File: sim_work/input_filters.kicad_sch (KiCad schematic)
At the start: 64 parts

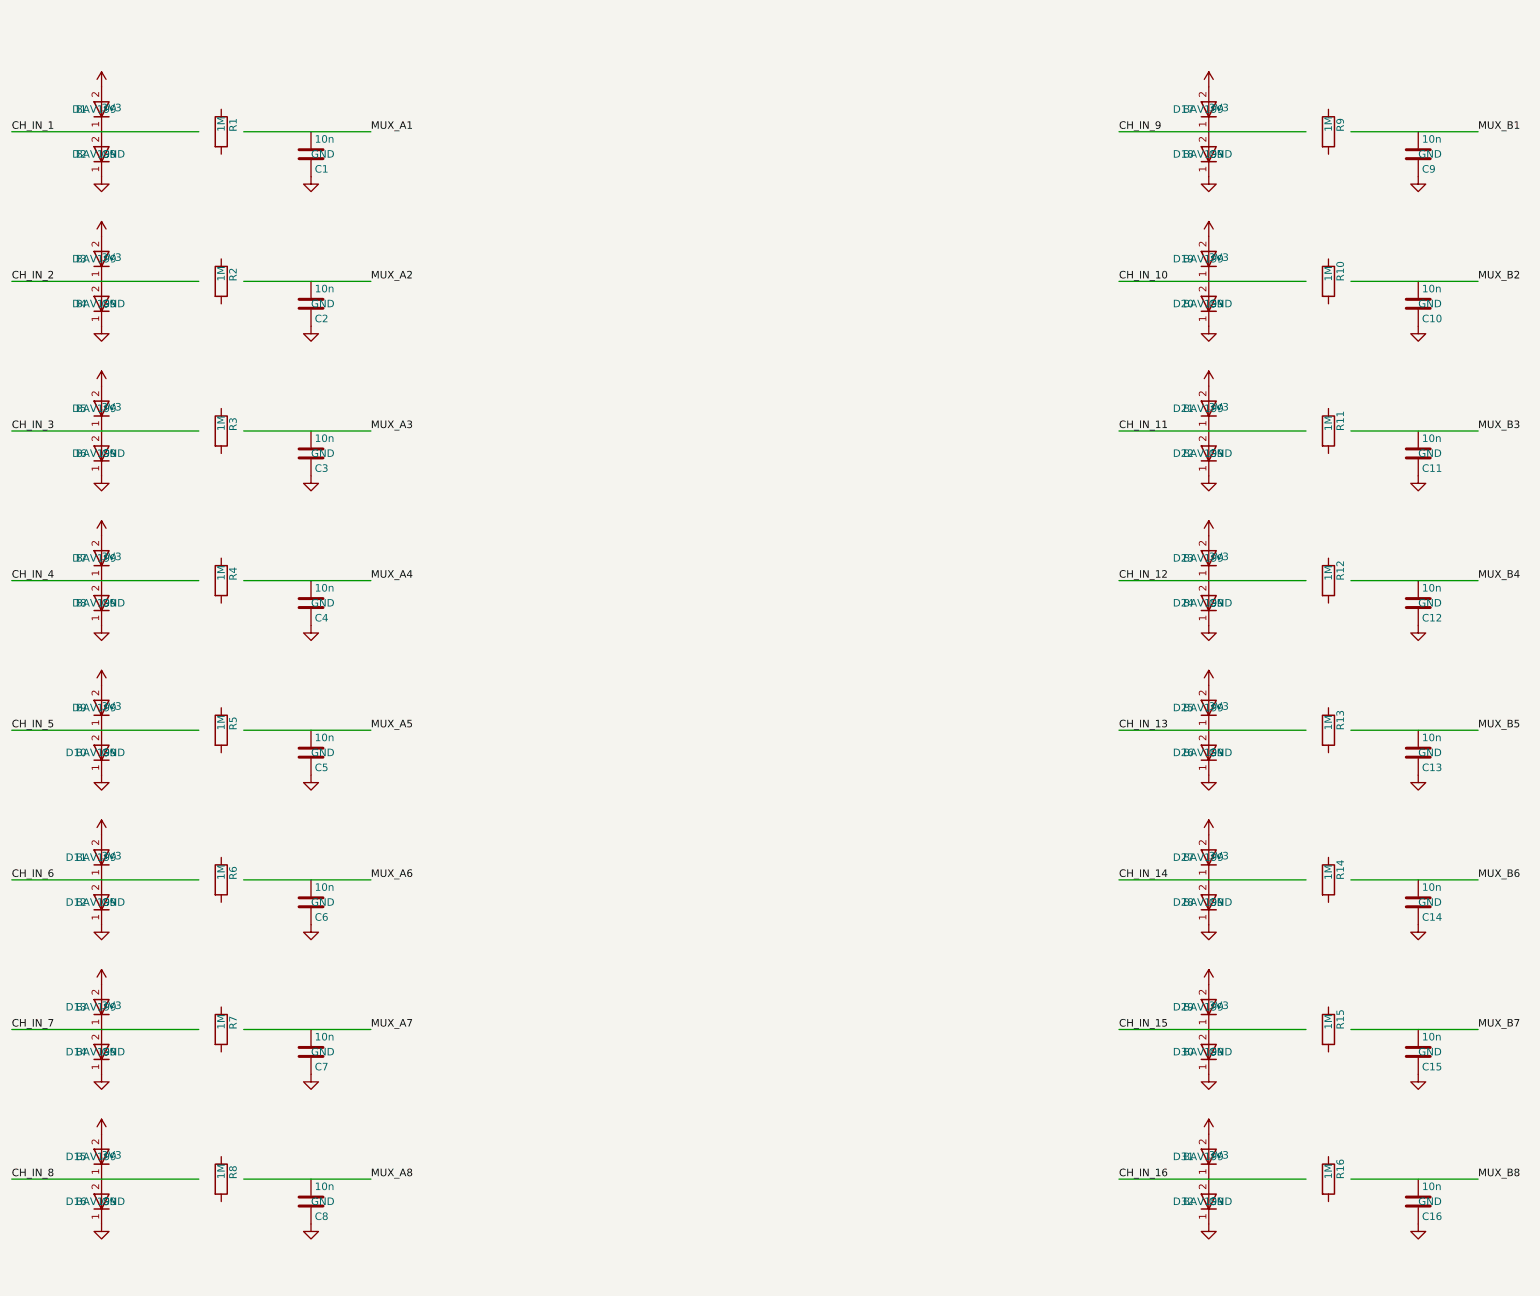
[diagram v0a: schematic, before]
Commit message: Per-block PDF schematics: 6 oscillator + 6 TIA blocks with merged PDFs
Add individual A4 schematic generation for each functional circuit block:
- Oscillator: summing amp, integrator 1/2, RMS detector, power supply, MCU
- TIA: input filters, analog mux, mux TIA, relay ladder, MCU section, electrometer
- merge_pdfs() helper using PyMuPDF for multi-page output
- CLI commands: osc_blocks, tia_blocks
- All blocks verified: 0 wire crossings, complete pin connectivity

Co-Authored-By: Claude Opus 4.6 <noreply@anthropic.com>
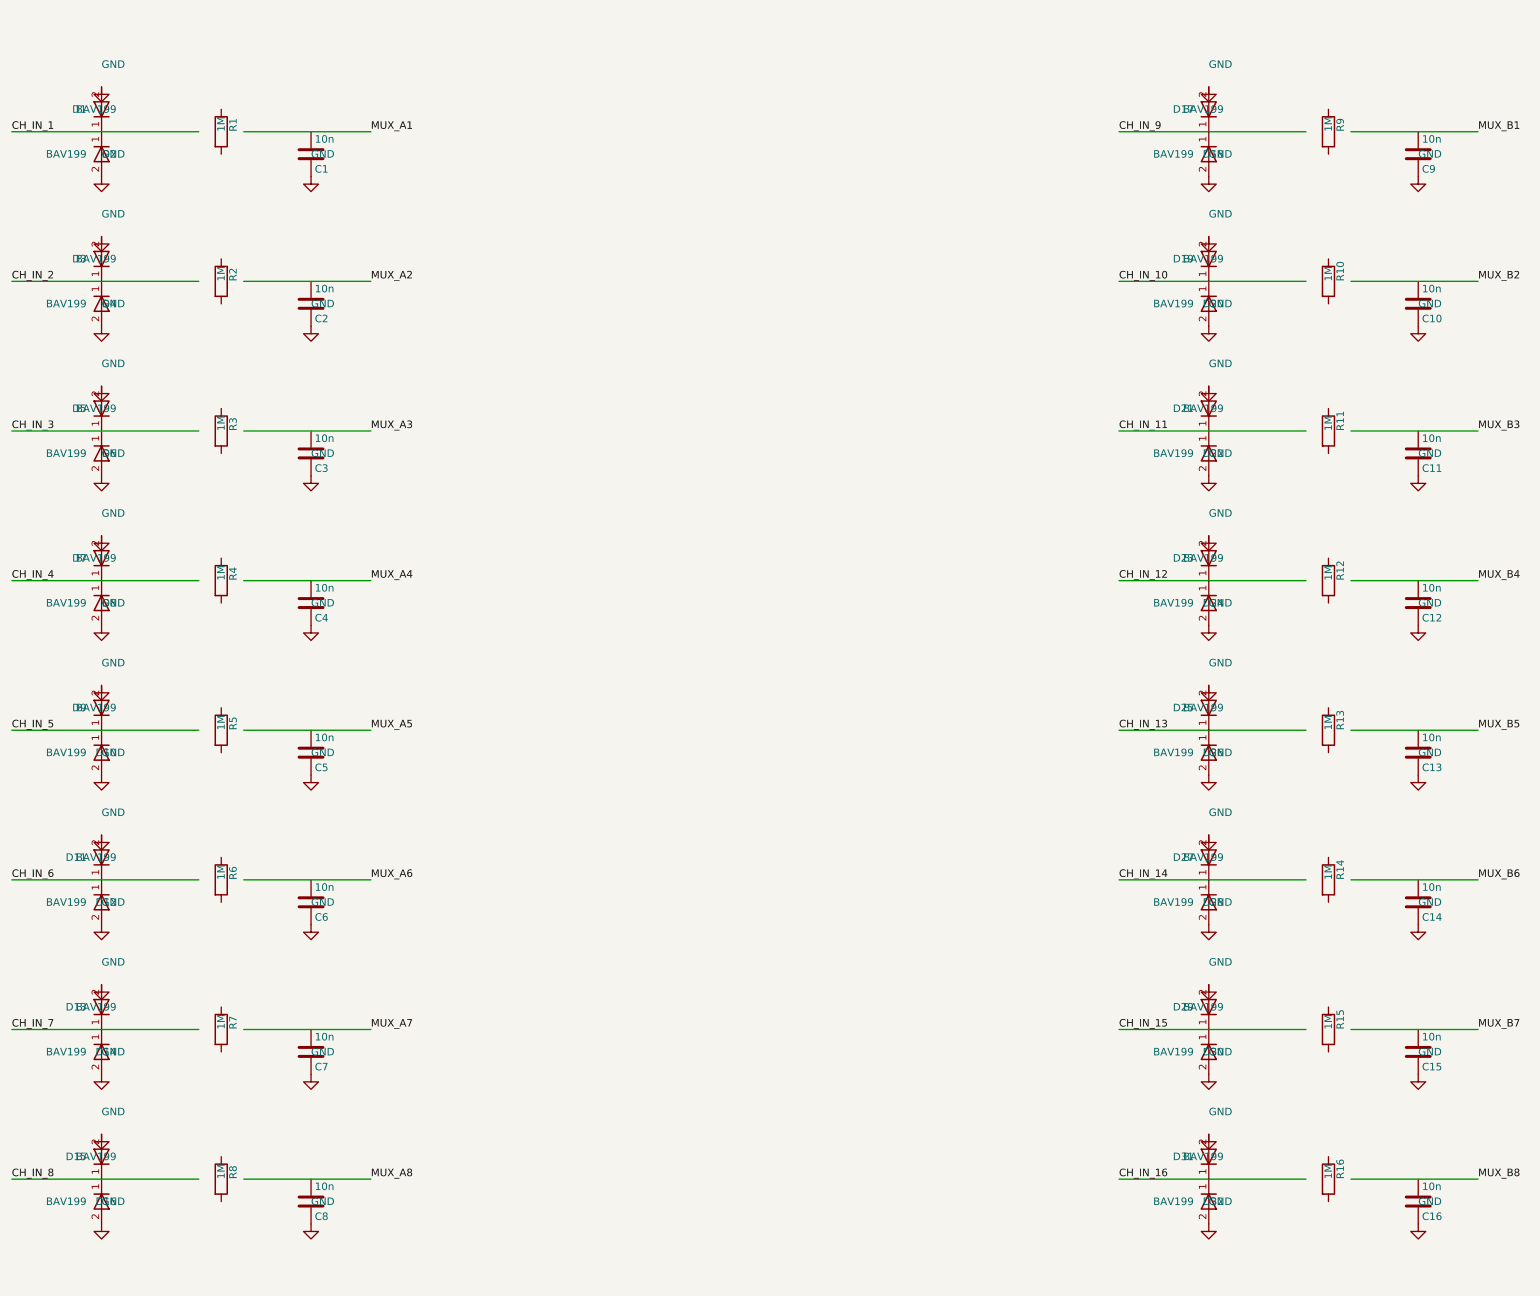
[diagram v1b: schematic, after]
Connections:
- net 3V3 is gone; now on net GND: D1.2 (A), D11.2 (A), D13.2 (A), D15.2 (A), D17.2 (A), D19.2 (A), D21.2 (A), D23.2 (A), D25.2 (A), D27.2 (A), D29.2 (A), D3.2 (A), D31.2 (A), D5.2 (A), D7.2 (A), D9.2 (A)
- net GND: now also D10.2 (A), D12.2 (A), D14.2 (A), D16.2 (A), D18.2 (A), D2.2 (A), D20.2 (A), D22.2 (A), D24.2 (A), D26.2 (A), D28.2 (A), D30.2 (A), D32.2 (A), D4.2 (A), D6.2 (A), D8.2 (A); no longer D10.1 (K), D12.1 (K), D14.1 (K), D16.1 (K), D18.1 (K), D2.1 (K), D20.1 (K), D22.1 (K), D24.1 (K), D26.1 (K), D28.1 (K), D30.1 (K), D32.1 (K), D4.1 (K), D6.1 (K), D8.1 (K)
- net at D15.1 (K): now also D16.1 (K); no longer D16.2 (A)
- net at D11.1 (K): now also D12.1 (K); no longer D12.2 (A)
- net at D21.1 (K): now also D22.1 (K); no longer D22.2 (A)
- net at D13.1 (K): now also D14.1 (K); no longer D14.2 (A)
- net at D1.1 (K): now also D2.1 (K); no longer D2.2 (A)
- net at D7.1 (K): now also D8.1 (K); no longer D8.2 (A)
- net at D19.1 (K): now also D20.1 (K); no longer D20.2 (A)
- net at D27.1 (K): now also D28.1 (K); no longer D28.2 (A)
- net at D23.1 (K): now also D24.1 (K); no longer D24.2 (A)
- net at D29.1 (K): now also D30.1 (K); no longer D30.2 (A)
- net at D9.1 (K): now also D10.1 (K); no longer D10.2 (A)
- net at D25.1 (K): now also D26.1 (K); no longer D26.2 (A)
- net at D31.1 (K): now also D32.1 (K); no longer D32.2 (A)
- net at D17.1 (K): now also D18.1 (K); no longer D18.2 (A)
- net at D3.1 (K): now also D4.1 (K); no longer D4.2 (A)
- net at D5.1 (K): now also D6.1 (K); no longer D6.2 (A)

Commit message: Fix schematic connections, add docs and repo portability
- Input filters: R rotation=90 (horizontal), ESD diode rotations fixed,
  junction dots at cathode-signal connection, wires to GND symbols
- Relay ladder: flyback diode rotation 270->90 (K top, A bottom)
- Electrometer/Mux TIA: 4 junction dots each at T-junctions
- AD636 RMS detector: proper IC box with pin labels replaces text-only
- Oscillator blocks: D_Zener symbol, L-shaped cathode routing
- TIA blocks: title/function annotations on all 5 blocks
- New: requirements.txt, docs/oscillator_guide.md
- D_Zener.kicad_sym added to bundled symbols/
- .gitignore updated for docs/ and requirements.txt
- README updated with pip install -r requirements.txt
- PROJECT.md session 9 changelog
- SimGUI builds clean (0 errors)

Co-Authored-By: Claude Opus 4.6 <noreply@anthropic.com>
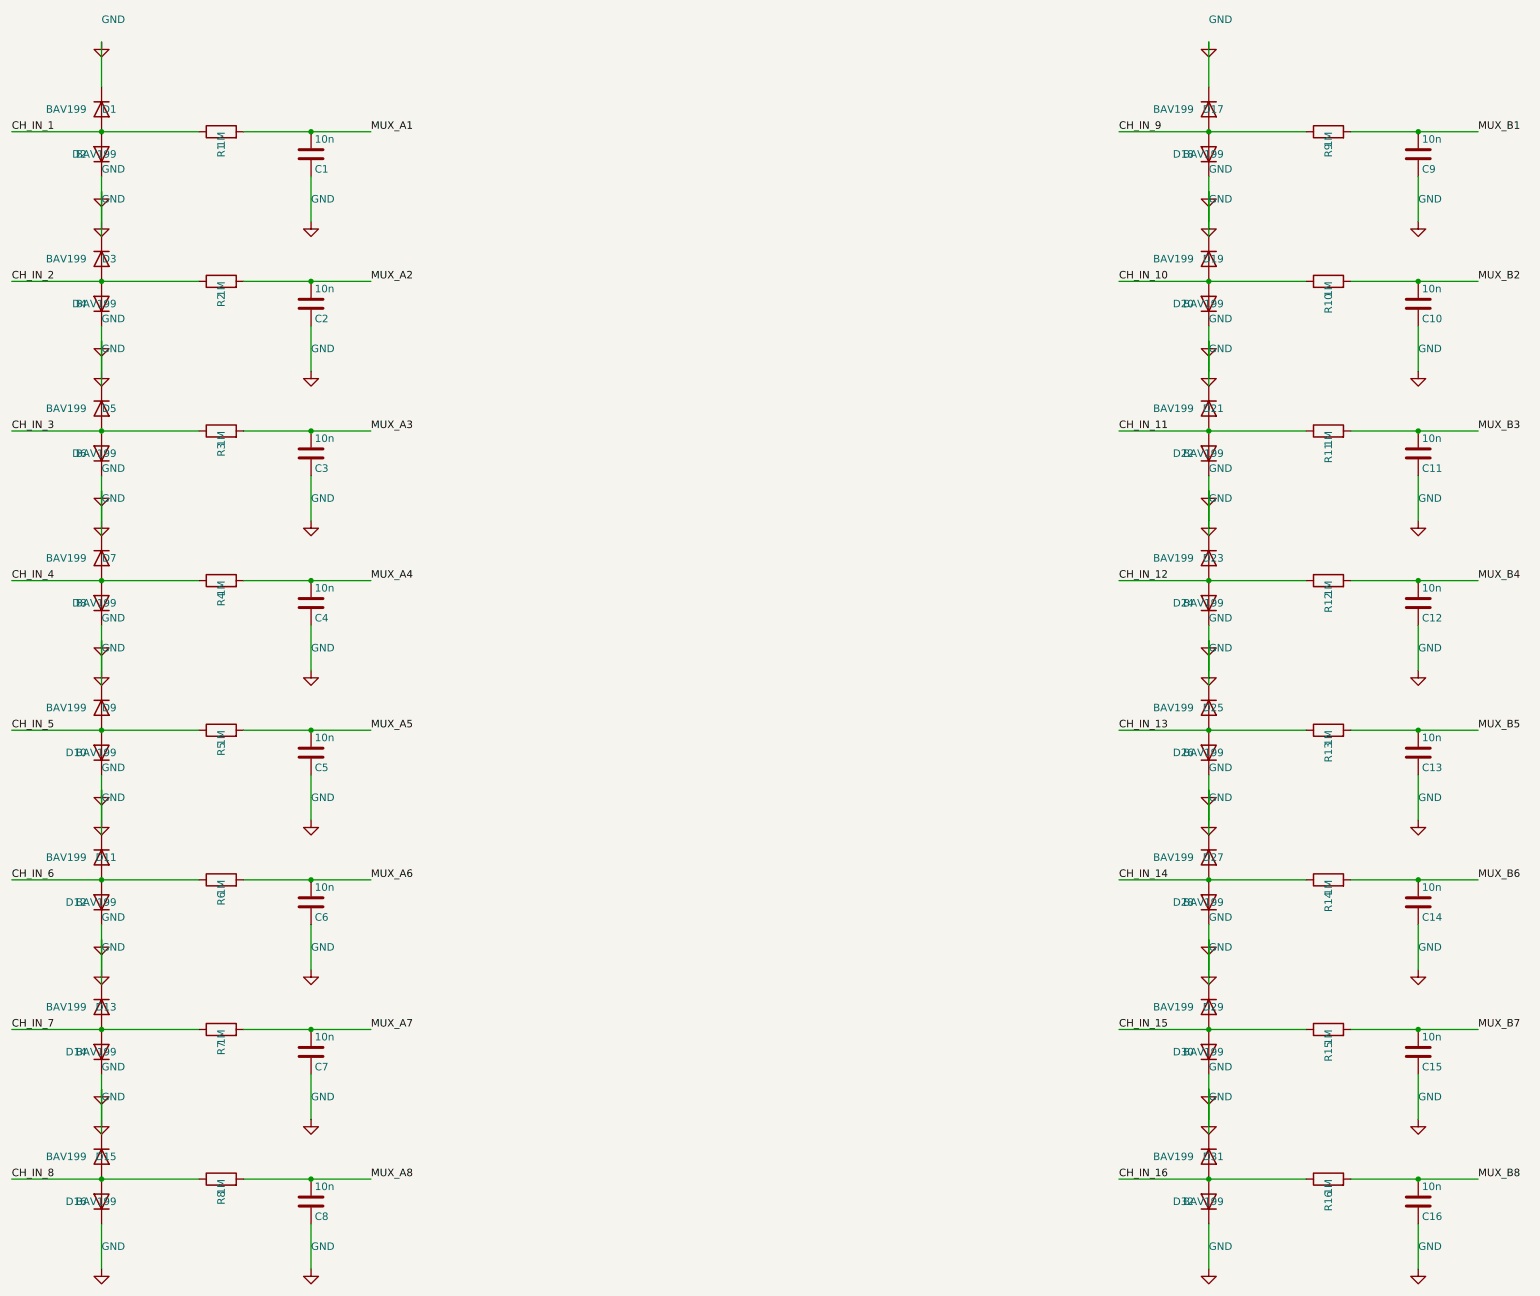
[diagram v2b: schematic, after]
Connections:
- net CH_IN_1: now also D1.2 (A), D2.2 (A), R1.1
- net CH_IN_10: now also D19.2 (A), D20.2 (A), R10.1
- net CH_IN_11: now also D21.2 (A), D22.2 (A), R11.1
- net CH_IN_12: now also D23.2 (A), D24.2 (A), R12.1
- net CH_IN_13: now also D25.2 (A), D26.2 (A), R13.1
- net CH_IN_14: now also D27.2 (A), D28.2 (A), R14.1
- net CH_IN_15: now also D29.2 (A), D30.2 (A), R15.1
- net CH_IN_16: now also D31.2 (A), D32.2 (A), R16.1
- net CH_IN_2: now also D3.2 (A), D4.2 (A), R2.1
- net CH_IN_3: now also D5.2 (A), D6.2 (A), R3.1
- net CH_IN_4: now also D7.2 (A), D8.2 (A), R4.1
- net CH_IN_5: now also D10.2 (A), D9.2 (A), R5.1
- net CH_IN_6: now also D11.2 (A), D12.2 (A), R6.1
- net CH_IN_7: now also D13.2 (A), D14.2 (A), R7.1
- net CH_IN_8: now also D15.2 (A), D16.2 (A), R8.1
- net CH_IN_9: now also D17.2 (A), D18.2 (A), R9.1
- net GND: now also D1.1 (K), D10.1 (K), D11.1 (K), D12.1 (K), D13.1 (K), D14.1 (K), D15.1 (K), D16.1 (K), D17.1 (K), D18.1 (K), D19.1 (K), D2.1 (K), D20.1 (K), D21.1 (K), D22.1 (K), D23.1 (K), D24.1 (K), D25.1 (K), D26.1 (K), D27.1 (K), D28.1 (K), D29.1 (K), D3.1 (K), D30.1 (K), D31.1 (K), D32.1 (K), D4.1 (K), D5.1 (K), D6.1 (K), D7.1 (K), D8.1 (K), D9.1 (K); no longer D1.2 (A), D10.2 (A), D11.2 (A), D12.2 (A), D13.2 (A), D14.2 (A), D15.2 (A), D16.2 (A), D17.2 (A), D18.2 (A), D19.2 (A), D2.2 (A), D20.2 (A), D21.2 (A), D22.2 (A), D23.2 (A), D24.2 (A), D25.2 (A), D26.2 (A), D27.2 (A), D28.2 (A), D29.2 (A), D3.2 (A), D30.2 (A), D31.2 (A), D32.2 (A), D4.2 (A), D5.2 (A), D6.2 (A), D7.2 (A), D8.2 (A), D9.2 (A)
- net MUX_A1: now also C1.1, R1.2
- net MUX_A2: now also C2.1, R2.2
- net MUX_A3: now also C3.1, R3.2
- net MUX_A4: now also C4.1, R4.2
- net MUX_A5: now also C5.1, R5.2
- net MUX_A6: now also C6.1, R6.2
- net MUX_A7: now also C7.1, R7.2
- net MUX_A8: now also C8.1, R8.2
- net MUX_B1: now also C9.1, R9.2
- net MUX_B2: now also C10.1, R10.2
- net MUX_B3: now also C11.1, R11.2
- net MUX_B4: now also C12.1, R12.2
- net MUX_B5: now also C13.1, R13.2
- net MUX_B6: now also C14.1, R14.2
- net MUX_B7: now also C15.1, R15.2
- net MUX_B8: now also C16.1, R16.2

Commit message: Tighten input filter layout: resistor closer to ESD diodes
Moved R from col_x+14G to col_x+9G (3.81mm gap vs 16.5mm) so the
diode-to-resistor connection is visually clear in rendered PDFs.
Capacitor and MUX label shifted left proportionally.

Co-Authored-By: Claude Opus 4.6 <noreply@anthropic.com>
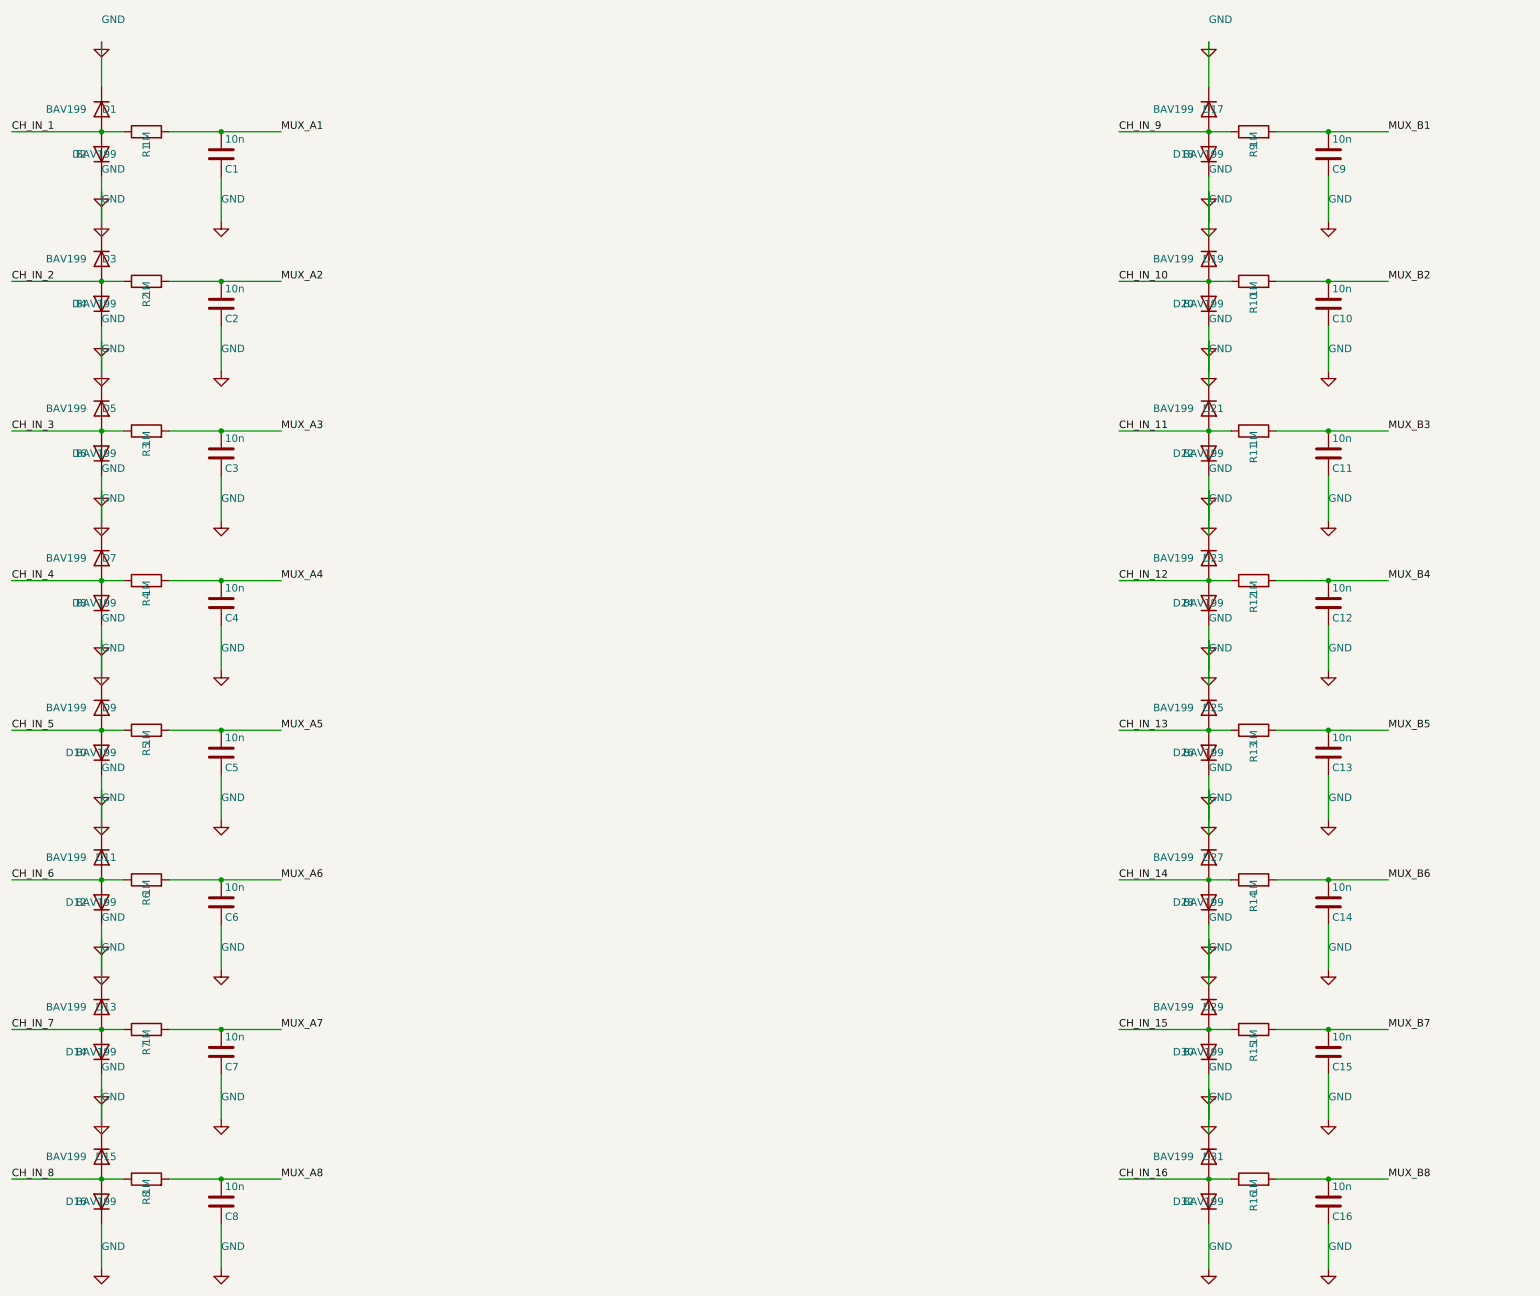
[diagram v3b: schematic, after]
